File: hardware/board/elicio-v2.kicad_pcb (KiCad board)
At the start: 2 copper layers, 35.5 x 53.7 mm, 66 parts, among them J1 TYPE-C-31-M-14, J2 SM02B-SRSS-TB, J3 HDR-3-RA, J4 TC2030-NL, P1 SIG1, P2 SIG2, P3 REF, Q1 AO3401A, Q2 2N7002, Q3 2N7002, Q4 2N7002, Q5 2N7002, SW1 4.5x4.5x1.6, U1 MDBT50Q-1MV2, U2 ADS1292IRSMT, U3 BQ25100YFPR, U4 TLV71330PDBVR, U5 USBLC6-2SC6

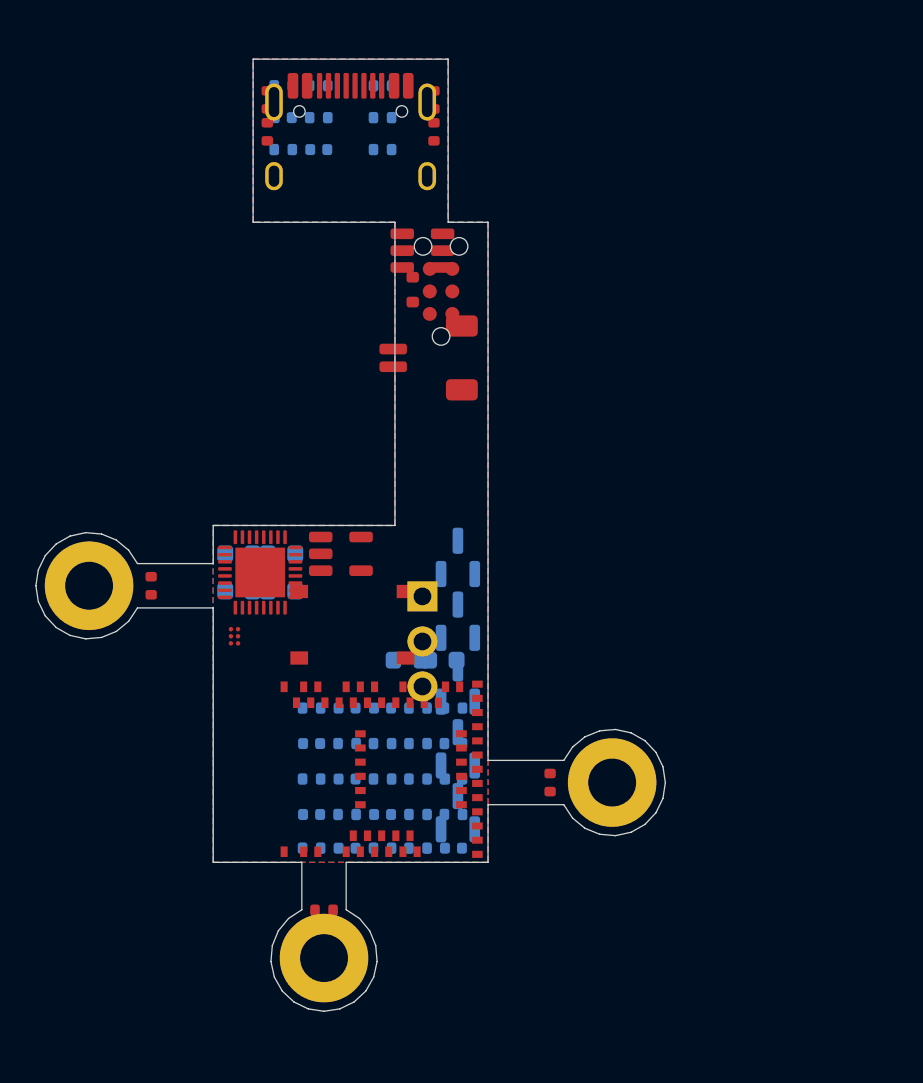
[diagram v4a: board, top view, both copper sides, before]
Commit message: board(v2d): width-22 outline and two-sided place from §5c
Pin from the no-receptacle table at e1f1d6f. R1–R3 on the island, holes at (13.45, 17.70) and (17.95, 17.70). Zero tracks. DRC 59 / unconnected 146. Routing waits on §5c final sha.

Co-authored-by: Cursor <cursoragent@cursor.com>
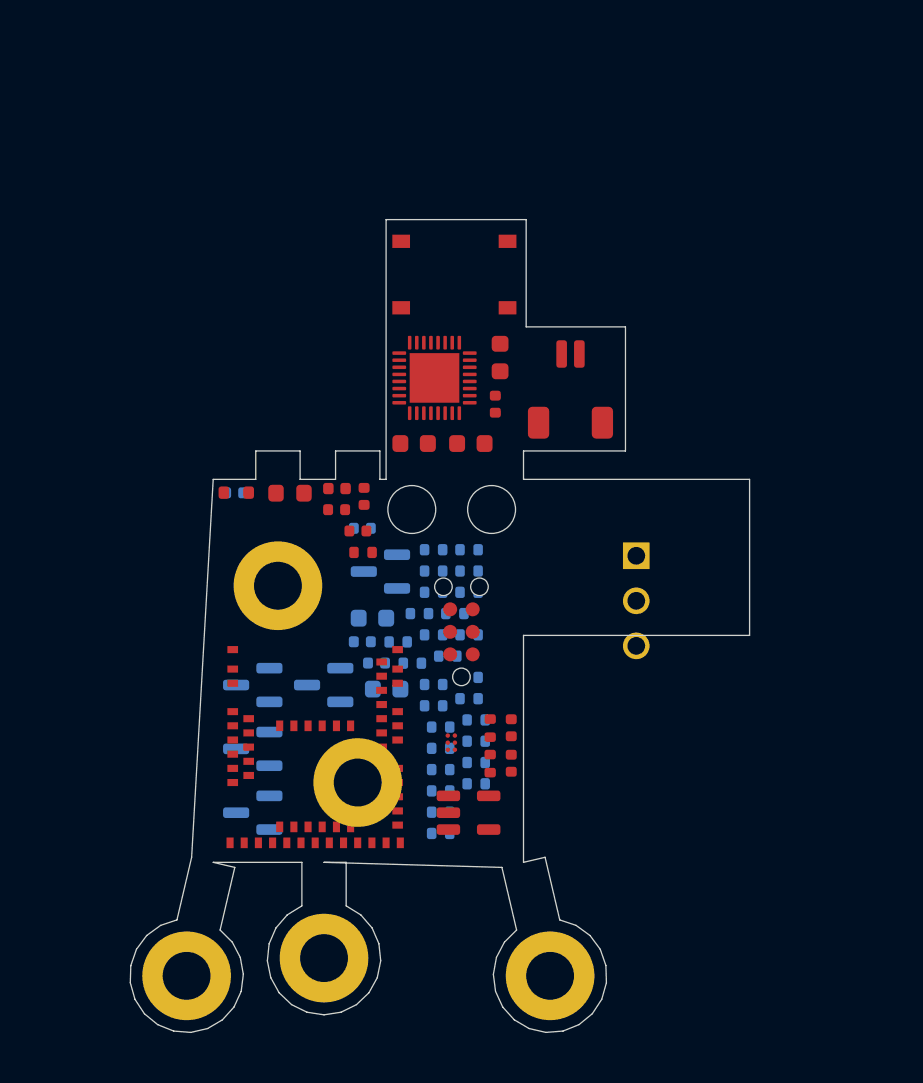
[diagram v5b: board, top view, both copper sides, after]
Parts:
- removed J1: TYPE-C-31-M-14, USB_C_Receptacle_HRO_TYPE-C-31-M-12
- removed U5: USBLC6-2SC6, SOT-23-6
- added H1: HOLE_D2.7, MountingHole_M2.5, F.Cu at (13.4, 17.7)
- added H2: HOLE_D2.7, MountingHole_M2.5, F.Cu at (17.9, 17.7)
- added P4: CHARGE_VBUS, RING_PAD_D5_H2.7, F.Cu at (0.75, 44.0)
- added P5: CHARGE_GND, RING_PAD_D5_H2.7, F.Cu at (21.2, 44.0)
- C1, C10, C2, C3, C4, C5, C6, C7, C8, D2, L1: moved to F.Cu
- R10, R18, R19, R9: moved to B.Cu
- moved R17 41.9 mm to (15.1, 34.8)
- moved R18 40.8 mm to (15.1, 36.0), turned to 180 degrees
- moved C5 38.6 mm to (19.1, 32.0), turned to 90 degrees
- moved R16 38.6 mm to (15.1, 33.6)
- moved R29 36.8 mm to (17.1, 32.0)
- moved R30 36.2 mm to (17.1, 33.2)
- moved R14 34.9 mm to (15.1, 31.2)
- moved C4 34.4 mm to (19.1, 30.0), turned to 90 degrees
- moved R5 32.6 mm to (13.5, 26.4)
- moved R10 30.2 mm to (14.7, 24.8), turned to 180 degrees
- moved R23 29.8 mm to (16.7, 22.4)
- moved R19 29.6 mm to (15.5, 26.0), turned to 180 degrees
- moved R9 29.3 mm to (14.7, 22.4), turned to 180 degrees
- moved C10 25.4 mm to (18.2, 11.8), turned to 90 degrees
- moved SW1 20.6 mm to (15.8, 4.45)
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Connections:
- J4 pad : NC-J4- -> (no net)
- R10 pad 1: CC2 -> unconnected-(R10-Pad1)
- R9 pad 1: CC1 -> unconnected-(R9-Pad1)
- U1 pad 34: USB_DN -> unconnected-(U1-D--Pad34)
- U1 pad 35: USB_DP -> unconnected-(U1-D+-Pad35)
- U2 pad : NC-U2- -> GND
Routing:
- removed copper zone on B.Cu, net GND
- removed copper zone on F.Cu, net GND
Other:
- board size 35.5 x 53.7 mm -> 34.9 x 45.8 mm
- board text added: "Eco1 FR4 0.4 #2 leftover/pocket"
- board text added: "NECK-END FOLD Q83 SIG1 10.71 SIG2 21.81"
- board text removed: "Eco1 FR4 0.4 #2 USB+pocket"
- board text removed: "NO TAB FR4; STANDOFF CLAMP Q58"

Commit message: board(v2d): re-pin from §5c final c6bd2fe
Vendor the no-receptacle width-22 pin table and rebuild the land. Hang outline grows so J3 pad 3 meets copper-to-edge 0.30. Tracks stay 0.

Co-authored-by: Cursor <cursoragent@cursor.com>
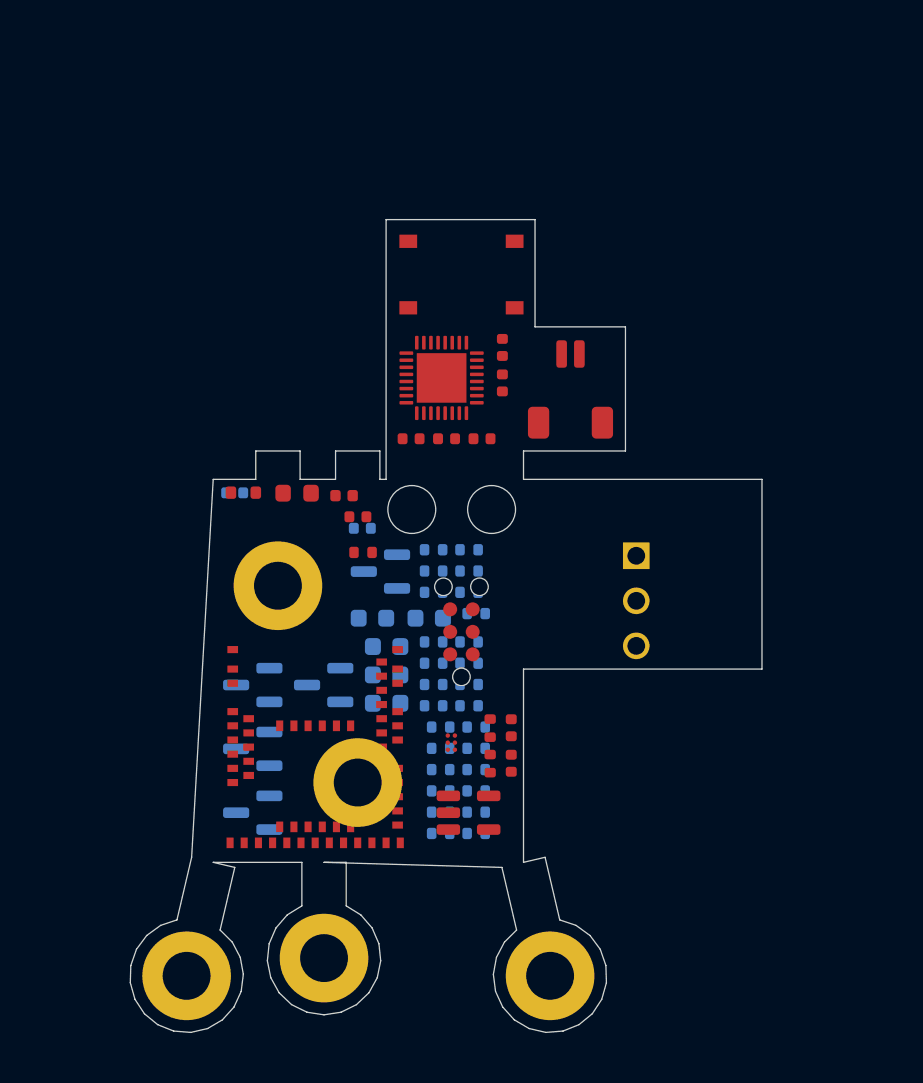
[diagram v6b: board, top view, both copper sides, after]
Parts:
- C11, C12: moved to F.Cu
- C6, C7, C8: moved to B.Cu
- moved C8 19.0 mm to (12.0, 27.0), turned to 180 degrees
- moved C5 18.7 mm to (15.4, 13.7), turned to 0 degrees
- moved C4 17.3 mm to (13.4, 13.7), turned to 0 degrees
- moved C3 17.2 mm to (19.1, 32.0)
- moved C11 17.2 mm to (18.6, 8.56), turned to 90 degrees
- moved R17 14.9 mm to (16.7, 20.0)
- moved R18 14.9 mm to (16.7, 21.2)
- moved C2 14.1 mm to (19.1, 30.0), turned to 90 degrees
- moved C7 12.4 mm to (12.0, 25.4), turned to 180 degrees
- moved C12 11.4 mm to (18.6, 10.6), turned to 90 degrees
- moved C13 11.1 mm to (3.46, 16.8)
- moved C6 10.1 mm to (11.2, 23.8), turned to 180 degrees
- moved C14 7.64 mm to (10.7, 18.8)
- moved R21 6.40 mm to (16.7, 26.4)
- moved R22 6.40 mm to (16.7, 27.6)
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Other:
- board size 34.9 x 45.8 mm -> 35.6 x 45.8 mm

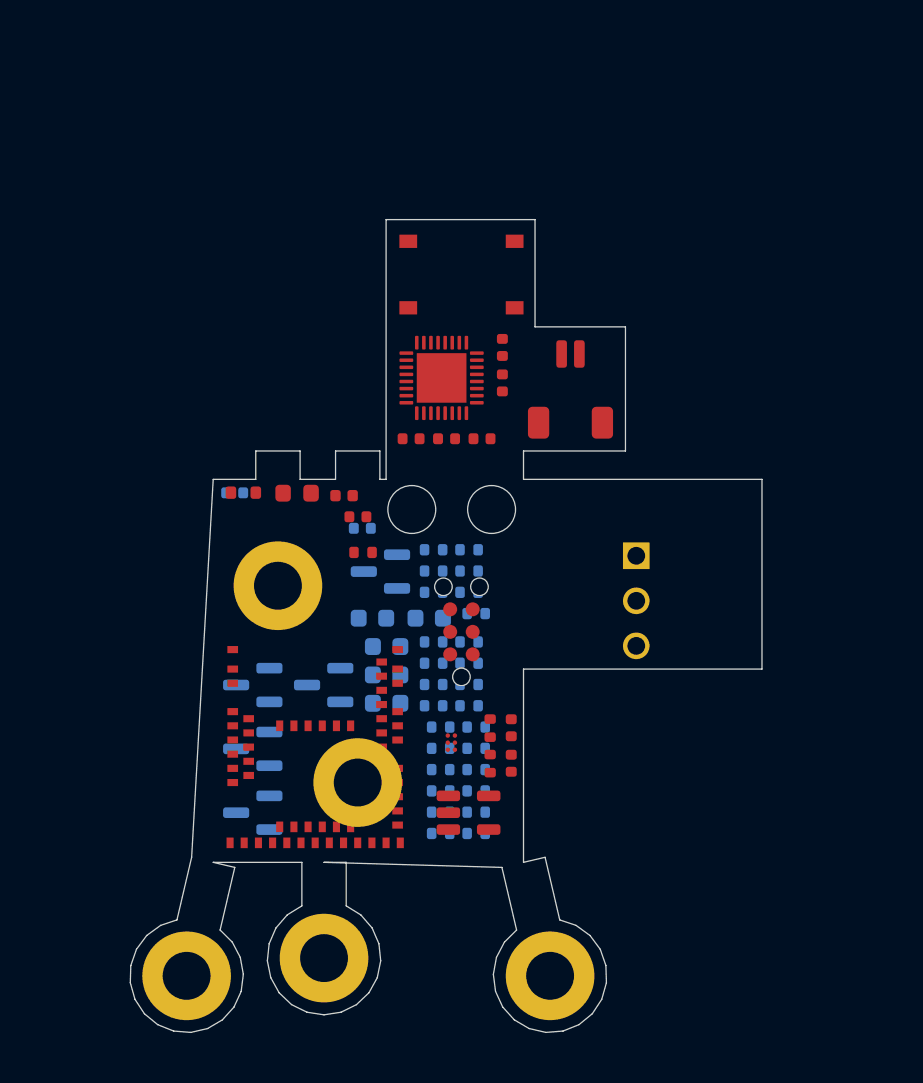
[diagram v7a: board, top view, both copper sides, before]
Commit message: board(v2e): placed on the flat pattern, not routed
Co-authored-by: Cursor <cursoragent@cursor.com>
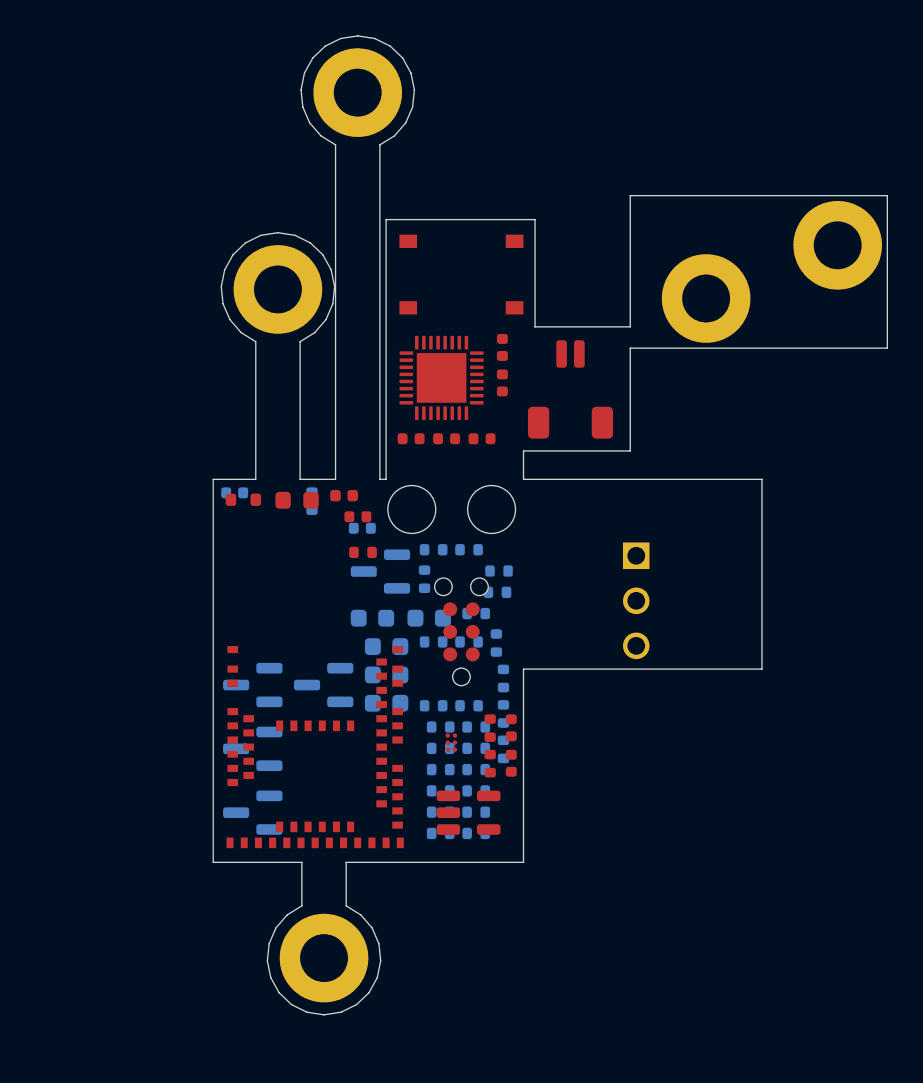
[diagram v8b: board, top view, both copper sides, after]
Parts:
- moved P4 55.2 mm to (37.5, 2.80)
- moved P5 39.2 mm to (30.1, 5.80)
- moved P2 38.9 mm to (10.4, -5.81)
- moved P1 16.7 mm to (5.90, 5.29)
- moved R25 15.7 mm to (7.82, 17.2), turned to 90 degrees
- moved R16 12.6 mm to (17.1, 23.6)
- moved R13 12.5 mm to (16.7, 20.0)
- moved R17 10.0 mm to (17.1, 30.0)
- moved R18 10.0 mm to (17.1, 31.2)
- moved R19 10.0 mm to (17.1, 32.4)
- moved R26 9.97 mm to (14.2, 21.6), turned to 90 degrees
- moved R14 8.55 mm to (16.7, 25.2)
- moved R21 8.41 mm to (17.1, 34.8)
- moved R20 8.41 mm to (17.1, 33.6)
- moved R22 8.41 mm to (17.1, 36.0)
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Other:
- board size 35.6 x 45.8 mm -> 38 x 55.2 mm
- board text added: "CHARGE TAB Q86"
- board text added: "SIG1 STRIP FLAT 10.71"
- board text added: "SIG2 STRIP FLAT 21.81"
- board text removed: "NECK BEND"
- board text removed: "NECK-END FOLD Q83 SIG1 10.71 SIG2 21.81"
